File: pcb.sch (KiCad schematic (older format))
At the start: 19 parts, among them J1 Conn_01x02, J2 Conn_01x03, J3 Conn_01x03, Q1 2N3904, Q2 2N3904, Q3 2N3904, Q4 2N3904, U1 STM32F103C8T6, U2 Shaft_encoder, U3 compass_accelerometer, U4 LM1117DT-3.3_NOPB, U5 3v7_to_5V_boost

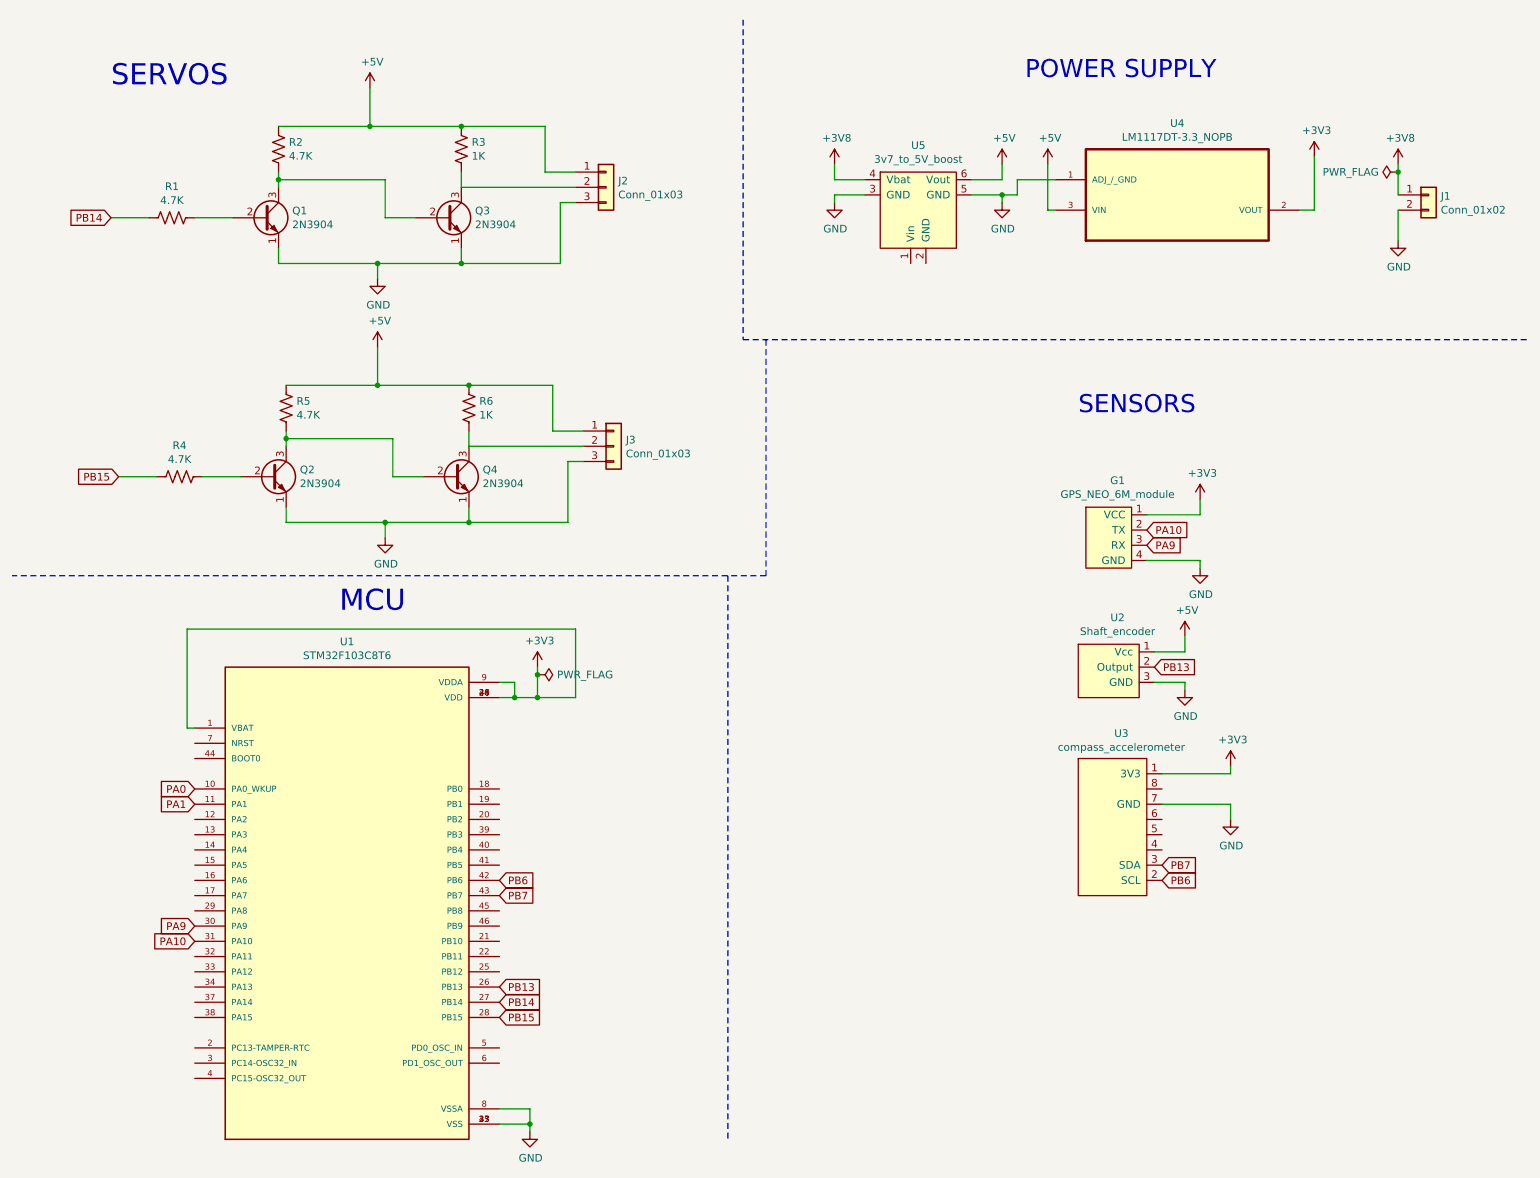
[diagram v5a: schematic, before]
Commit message: changed 3v3 symbol
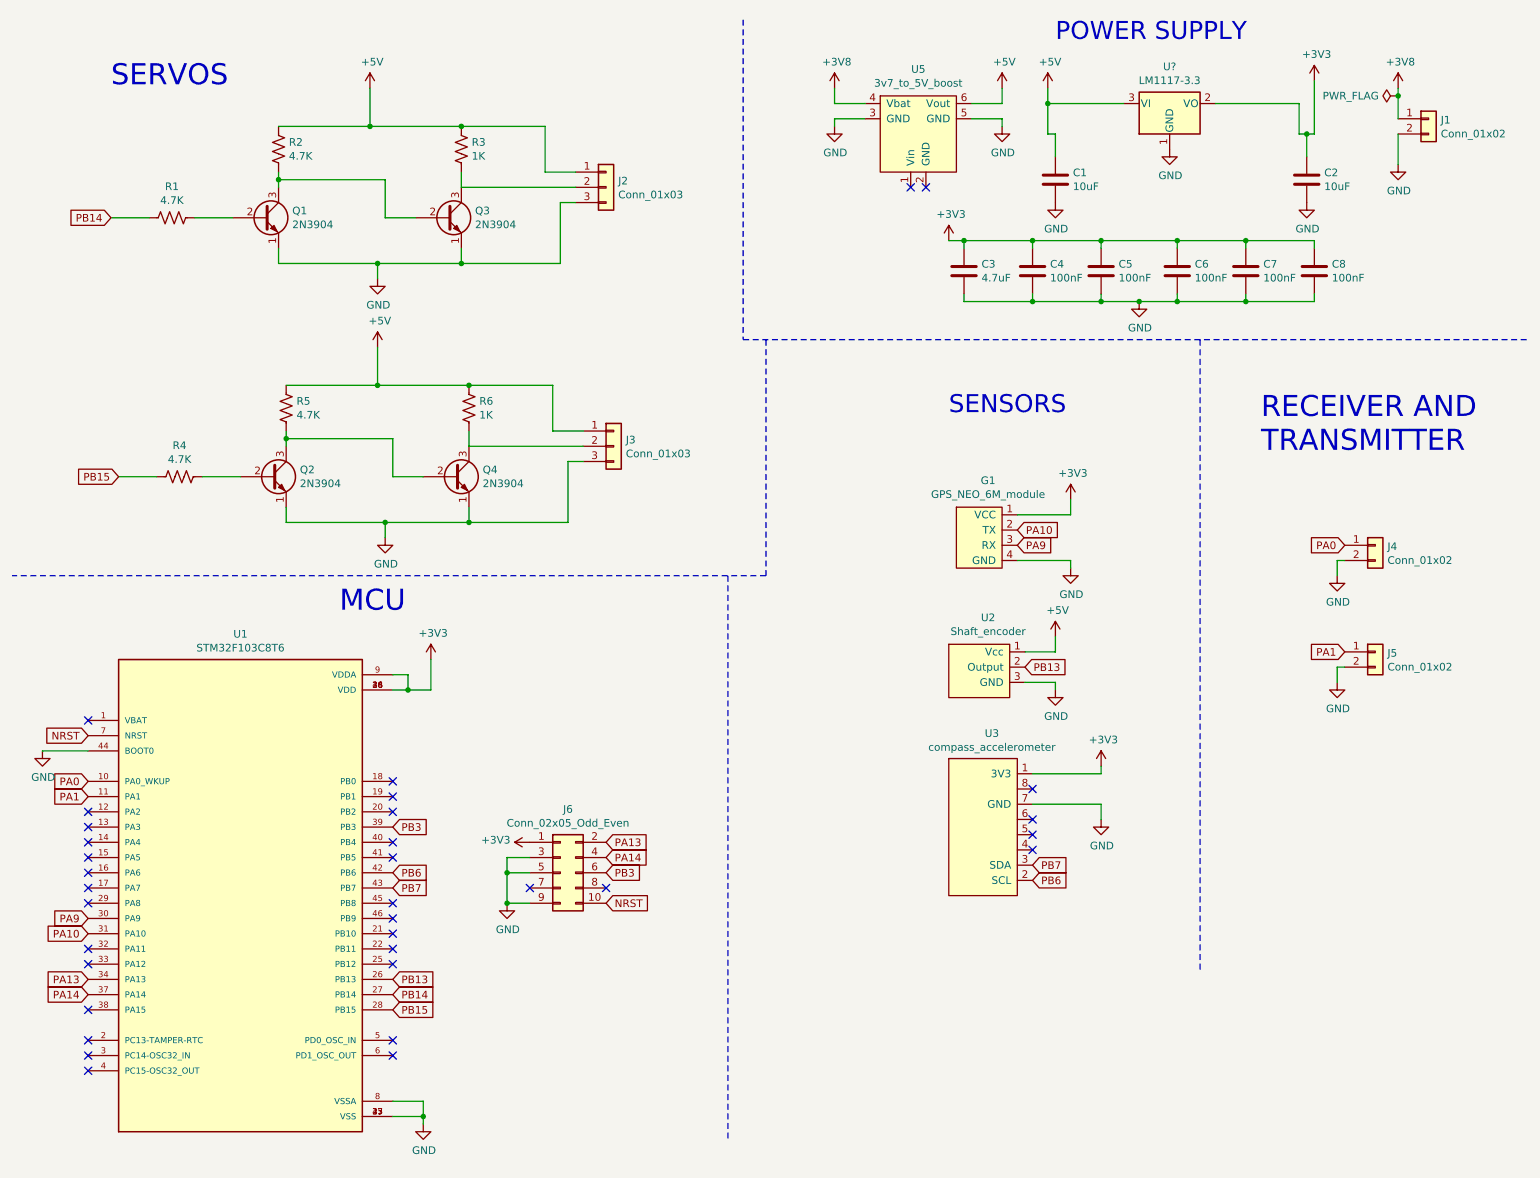
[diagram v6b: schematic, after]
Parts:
- removed U4: LM1117DT-3.3_NOPB, LM1117DT-3_1:TO228P970X238-3N, symbol LM1117DT-3.3_NOPB:LM1117DT-3.3_NOPB
- added C1, C2: 10uF, symbol device:C
- added C3: 4.7uF, symbol device:C
- added C4, C5, C6, C7, C8: 100nF, symbol device:C
- added J4, J5: Conn_01x02, symbol Connector_Generic:Conn_01x02
- added J6: Conn_02x05_Odd_Even, symbol Connector_Generic:Conn_02x05_Odd_Even
- added U?: LM1117-3.3, symbol Regulator_Linear:LM1117-3.3
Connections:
- net +3V3: now also C2.1, C3.1, C4.1, C5.1, C6.1, C7.1, C8.1, J6.1 (Pin_1), U?.2 (VO); no longer U1.1 (VBAT)
- net +5V: now also C1.1, U?.3 (VI)
- net GND: now also U1.44 (BOOT0), C1.2, C2.2, C3.2, C4.2, C5.2, C6.2, C7.2, C8.2, J4.2 (Pin_2), J5.2 (Pin_2), J6.3 (Pin_3), J6.5 (Pin_5), J6.9 (Pin_9), U?.1 (GND)
- net PA0: now also J4.1 (Pin_1)
- net PA1: now also J5.1 (Pin_1)
- net PA13: now reaches U1.34 (PA13)
- net PA13: now also J6.2 (Pin_2)
- net PA14: now reaches U1.37 (PA14)
- net PA14: now also J6.4 (Pin_4)
- net PB3: now reaches U1.39 (PB3)
- net PB3: now also J6.6 (Pin_6)
- net NRST: now reaches U1.7 (NRST)
- net NRST: now also J6.10 (Pin_10)
- no-connect marks 0 -> 34
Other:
- note added: "RECEIVER AND\nTRANSMITTER"
- moved on the sheet: G1, J1, U1, U2, U3, U5

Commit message: I do not remember what I changed
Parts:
- gave numbers to parts that had none: 1
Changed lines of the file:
@@
 $EndComp
 $Comp
-L Regulator_Linear:LM1117-3.3 U?
+L Regulator_Linear:LM1117-3.3 U4
 U 1 1 62158C27
 P 8150 1050
-F 0 "U?" H 8150 1292 50  0000 C CNN
+F 0 "U4" H 8150 1292 50  0000 C CNN
 F 1 "LM1117-3.3" H 8150 1201 50  0000 C CNN
 F 2 "" H 8150 1050 50  0001 C CNN
@@
 	9000 1050 9000 1250
 $Comp
-L power:GND #PWR?
+L power:GND #PWR018
 U 1 1 6216B3AE
 P 8150 1350
-F 0 "#PWR?" H 8150 1100 50  0001 C CNN
+F 0 "#PWR018" H 8150 1100 50  0001 C CNN
 F 1 "GND" H 8155 1177 50  0000 C CNN
 F 2 "" H 8150 1350 50  0001 C CNN

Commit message: started layout
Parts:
- C1, C2: footprint (none) -> Capacitor_SMD:C_0805_2012Metric_Pad1.15x1.40mm_HandSolder
- C3, C4, C5, C6, C7, C8: footprint (none) -> Capacitor_SMD:C_0603_1608Metric_Pad1.05x0.95mm_HandSolder
- J1, J4, J5: footprint (none) -> Connector_PinHeader_2.54mm:PinHeader_1x02_P2.54mm_Vertical
- J2, J3: footprint (none) -> Connector_PinHeader_2.54mm:PinHeader_1x03_P2.54mm_Vertical
- J6: footprint (none) -> Connector_PinHeader_2.54mm:PinHeader_2x05_P2.54mm_Vertical
- R1, R2, R3, R4, R5, R6: footprint (none) -> Resistor_SMD:R_1206_3216Metric_Pad1.42x1.75mm_HandSolder
- U4: footprint (none) -> LM1117DT-3_1:TO228P970X238-3N
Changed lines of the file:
@@
 F 0 "J1" H 9930 1142 50  0000 L CNN
 F 1 "Conn_01x02" H 9930 1051 50  0000 L CNN
-F 2 "" H 9850 1150 50  0001 C CNN
+F 2 "Connector_PinHeader_2.54mm:PinHeader_1x02_P2.54mm_Vertical" H 9850 1150 50  0001 C CNN
 F 3 "~" H 9850 1150 50  0001 C CNN
 	1    9850 1150
@@
 F 0 "R1" V 1395 1800 50  0000 C CNN
 F 1 "4.7K" V 1486 1800 50  0000 C CNN
-F 2 "" V 1640 1790 50  0001 C CNN
+F 2 "Resistor_SMD:R_1206_3216Metric_Pad1.42x1.75mm_HandSolder" V 1640 1790 50  0001 C CNN
 F 3 "~" H 1600 1800 50  0001 C CNN
 	1    1600 1800
@@
 F 0 "R2" H 2368 1396 50  0000 L CNN
 F 1 "4.7K" H 2368 1305 50  0000 L CNN
-F 2 "" V 2340 1340 50  0001 C CNN
+F 2 "Resistor_SMD:R_1206_3216Metric_Pad1.42x1.75mm_HandSolder" V 2340 1340 50  0001 C CNN
 F 3 "~" H 2300 1350 50  0001 C CNN
 	1    2300 1350
@@
 F 0 "R3" H 3568 1396 50  0000 L CNN
 F 1 "1K" H 3568 1305 50  0000 L CNN
-F 2 "" V 3540 1340 50  0001 C CNN
+F 2 "Resistor_SMD:R_1206_3216Metric_Pad1.42x1.75mm_HandSolder" V 3540 1340 50  0001 C CNN
 F 3 "~" H 3500 1350 50  0001 C CNN
 	1    3500 1350
@@
 F 0 "J2" H 4530 1642 50  0000 L CNN
 F 1 "Conn_01x03" H 4530 1551 50  0000 L CNN
-F 2 "" H 4450 1600 50  0001 C CNN
+F 2 "Connector_PinHeader_2.54mm:PinHeader_1x03_P2.54mm_Vertical" H 4450 1600 50  0001 C CNN
 F 3 "~" H 4450 1600 50  0001 C CNN
 	1    4450 1600
@@
 F 0 "J3" H 4580 3342 50  0000 L CNN
 F 1 "Conn_01x03" H 4580 3251 50  0000 L CNN
-F 2 "" H 4500 3300 50  0001 C CNN
+F 2 "Connector_PinHeader_2.54mm:PinHeader_1x03_P2.54mm_Vertical" H 4500 3300 50  0001 C CNN
 F 3 "~" H 4500 3300 50  0001 C CNN
 	1    4500 3300
@@
 F 0 "R6" H 3618 3096 50  0000 L CNN
 F 1 "1K" H 3618 3005 50  0000 L CNN
-F 2 "" V 3590 3040 50  0001 C CNN
+F 2 "Resistor_SMD:R_1206_3216Metric_Pad1.42x1.75mm_HandSolder" V 3590 3040 50  0001 C CNN
 F 3 "~" H 3550 3050 50  0001 C CNN
 	1    3550 3050
@@
 F 0 "R5" H 2418 3096 50  0000 L CNN
 F 1 "4.7K" H 2418 3005 50  0000 L CNN
-F 2 "" V 2390 3040 50  0001 C CNN
+F 2 "Resistor_SMD:R_1206_3216Metric_Pad1.42x1.75mm_HandSolder" V 2390 3040 50  0001 C CNN
 F 3 "~" H 2350 3050 50  0001 C CNN
 	1    2350 3050
@@
 F 0 "R4" V 1445 3500 50  0000 C CNN
 F 1 "4.7K" V 1536 3500 50  0000 C CNN
-F 2 "" V 1690 3490 50  0001 C CNN
+F 2 "Resistor_SMD:R_1206_3216Metric_Pad1.42x1.75mm_HandSolder" V 1690 3490 50  0001 C CNN
 F 3 "~" H 1650 3500 50  0001 C CNN
 	1    1650 3500
@@
 F 0 "J4" H 9580 3942 50  0000 L CNN
 F 1 "Conn_01x02" H 9580 3851 50  0000 L CNN
-F 2 "" H 9500 3950 50  0001 C CNN
+F 2 "Connector_PinHeader_2.54mm:PinHeader_1x02_P2.54mm_Vertical" H 9500 3950 50  0001 C CNN
 F 3 "~" H 9500 3950 50  0001 C CNN
 	1    9500 3950
@@
 F 0 "J5" H 9580 4642 50  0000 L CNN
 F 1 "Conn_01x02" H 9580 4551 50  0000 L CNN
-F 2 "" H 9500 4650 50  0001 C CNN
+F 2 "Connector_PinHeader_2.54mm:PinHeader_1x02_P2.54mm_Vertical" H 9500 4650 50  0001 C CNN
 F 3 "~" H 9500 4650 50  0001 C CNN
 	1    9500 4650
@@
 F 0 "C2" H 9165 1596 50  0000 L CNN
 F 1 "10uF" H 9165 1505 50  0000 L CNN
-F 2 "" H 9088 1400 50  0001 C CNN
+F 2 "Capacitor_SMD:C_0805_2012Metric_Pad1.15x1.40mm_HandSolder" H 9088 1400 50  0001 C CNN
 F 3 "~" H 9050 1550 50  0001 C CNN
 	1    9050 1550
@@
 F 0 "C1" H 7515 1596 50  0000 L CNN
 F 1 "10uF" H 7515 1505 50  0000 L CNN
-F 2 "" H 7438 1400 50  0001 C CNN
+F 2 "Capacitor_SMD:C_0805_2012Metric_Pad1.15x1.40mm_HandSolder" H 7438 1400 50  0001 C CNN
 F 3 "~" H 7400 1550 50  0001 C CNN
 	1    7400 1550
@@
 F 0 "C5" H 7815 2196 50  0000 L CNN
 F 1 "100nF" H 7815 2105 50  0000 L CNN
-F 2 "" H 7738 2000 50  0001 C CNN
+F 2 "Capacitor_SMD:C_0603_1608Metric_Pad1.05x0.95mm_HandSolder" H 7738 2000 50  0001 C CNN
 F 3 "~" H 7700 2150 50  0001 C CNN
 	1    7700 2150
@@
 F 0 "C6" H 8315 2196 50  0000 L CNN
 F 1 "100nF" H 8315 2105 50  0000 L CNN
-F 2 "" H 8238 2000 50  0001 C CNN
+F 2 "Capacitor_SMD:C_0603_1608Metric_Pad1.05x0.95mm_HandSolder" H 8238 2000 50  0001 C CNN
 F 3 "~" H 8200 2150 50  0001 C CNN
 	1    8200 2150
@@
 F 0 "C7" H 8765 2196 50  0000 L CNN
 F 1 "100nF" H 8765 2105 50  0000 L CNN
-F 2 "" H 8688 2000 50  0001 C CNN
+F 2 "Capacitor_SMD:C_0603_1608Metric_Pad1.05x0.95mm_HandSolder" H 8688 2000 50  0001 C CNN
 F 3 "~" H 8650 2150 50  0001 C CNN
 	1    8650 2150
@@
 F 0 "C8" H 9215 2196 50  0000 L CNN
 F 1 "100nF" H 9215 2105 50  0000 L CNN
-F 2 "" H 9138 2000 50  0001 C CNN
+F 2 "Capacitor_SMD:C_0603_1608Metric_Pad1.05x0.95mm_HandSolder" H 9138 2000 50  0001 C CNN
 F 3 "~" H 9100 2150 50  0001 C CNN
 	1    9100 2150
@@
 F 0 "C4" H 7365 2196 50  0000 L CNN
 F 1 "100nF" H 7365 2105 50  0000 L CNN
-F 2 "" H 7288 2000 50  0001 C CNN
+F 2 "Capacitor_SMD:C_0603_1608Metric_Pad1.05x0.95mm_HandSolder" H 7288 2000 50  0001 C CNN
 F 3 "~" H 7250 2150 50  0001 C CNN
 	1    7250 2150
@@
 F 0 "C3" H 6915 2196 50  0000 L CNN
 F 1 "4.7uF" H 6915 2105 50  0000 L CNN
-F 2 "" H 6838 2000 50  0001 C CNN
+F 2 "Capacitor_SMD:C_0603_1608Metric_Pad1.05x0.95mm_HandSolder" H 6838 2000 50  0001 C CNN
 F 3 "~" H 6800 2150 50  0001 C CNN
 	1    6800 2150
@@
 F 0 "J6" H 4200 6517 50  0000 C CNN
 F 1 "Conn_02x05_Odd_Even" H 4200 6426 50  0000 C CNN
-F 2 "" H 4150 6100 50  0001 C CNN
+F 2 "Connector_PinHeader_2.54mm:PinHeader_2x05_P2.54mm_Vertical" H 4150 6100 50  0001 C CNN
 F 3 "~" H 4150 6100 50  0001 C CNN
 	1    4150 6100
@@
 F 0 "U4" H 8150 1292 50  0000 C CNN
 F 1 "LM1117-3.3" H 8150 1201 50  0000 C CNN
-F 2 "" H 8150 1050 50  0001 C CNN
+F 2 "LM1117DT-3_1:TO228P970X238-3N" H 8150 1050 50  0001 C CNN
 F 3 "http://www.ti.com/lit/ds/symlink/lm1117.pdf" H 8150 1050 50  0001 C CNN
 	1    8150 1050
